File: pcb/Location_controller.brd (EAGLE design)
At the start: 75 x 48 mm, 45 parts, among them IC1 LIS302DL

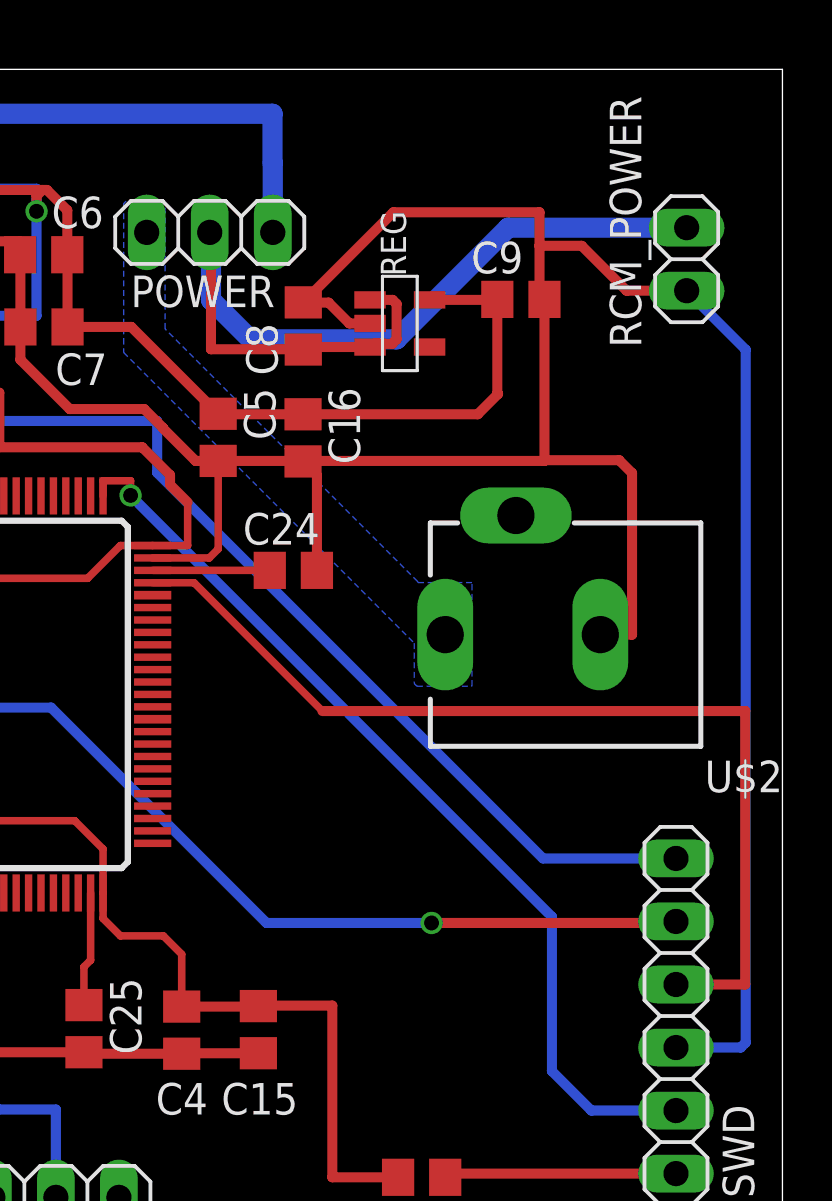
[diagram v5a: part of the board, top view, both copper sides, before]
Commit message: Add PWR and ERR indicator LEDs
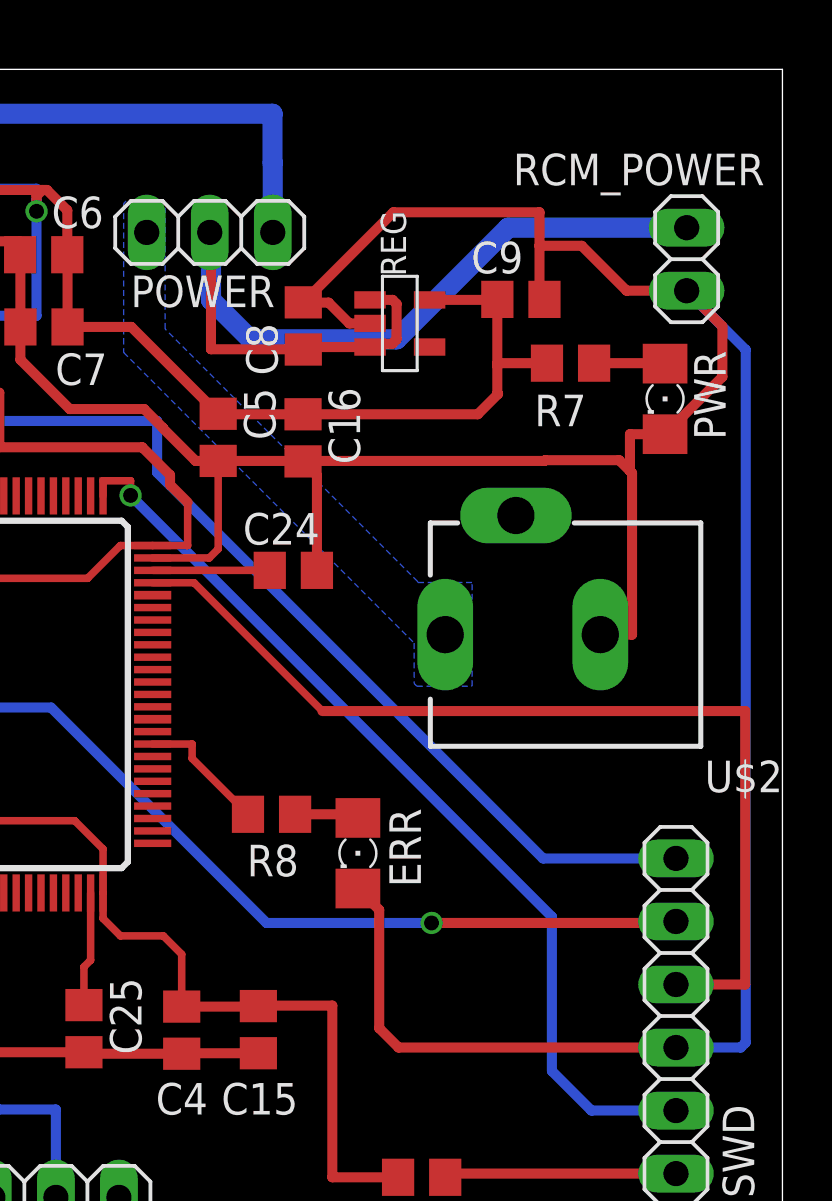
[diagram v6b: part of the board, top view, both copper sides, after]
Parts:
- added ERR, PWR: (no value), eagle-ltspice:LED_1206
- added R7, R8: 68, eagle-ltspice:R0805
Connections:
- new net N$12: PWR.A, R7.1
- new net N$13: ERR.A, R8.1
- new net N$14: R8.2, U$1.59
- net GND: now also ERR.C, PWR.C
- net VDD: now also R7.2
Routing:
- net GND: track 324.7 -> 346.7 mm
- net N$14: track 0.00 -> 5.35 mm
- net N$12: track 0.00 -> 2.88 mm
- net N$13: track 0.00 -> 2.59 mm
- net VDD: track 272.9 -> 274.9 mm
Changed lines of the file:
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@@
 </element>
 <element name="RCM_POWER" library="pinhead" package="1X02" value="" x="71.14" y="40.35" smashed="yes" rot="R90">
-<attribute name="NAME" x="69.3112" y="36.7938" size="1.27" layer="25" ratio="10" rot="R90"/>
+<attribute name="NAME" x="74.2762" y="44.6012" size="1.27" layer="25" ratio="10" rot="R180"/>
 <attribute name="VALUE" x="74.315" y="37.81" size="1.27" layer="27" rot="R90"/>
 </element>
@@
 <element name="JP2" library="pinhead" package="1X06" value="" x="25.4" y="2.54"/>
 <element name="JP3" library="pinhead" package="1X06" value="" x="8.89" y="2.54"/>
+<element name="PWR" library="eagle-ltspice" package="LED_1206" value="" x="70.27" y="34.72" smashed="yes" rot="R270">
+<attribute name="SPICEMODEL" value="NONE" x="70.27" y="34.72" size="1.778" layer="27" rot="R270" display="off"/>
+<attribute name="SPICETYPE" value="diode" x="70.27" y="34.72" size="1.778" layer="27" rot="R270" display="off"/>
+<attribute name="SPICEPREFIX" value="D" x="70.27" y="34.72" size="1.778" layer="27" rot="R270" display="off"/>
+<attribute name="NAME" x="71.44" y="36.66" size="1.27" layer="25" rot="R270"/>
+<attribute name="VALUE" x="67.73" y="35.99" size="1.27" layer="27" rot="R270"/>
+</element>
+<element name="R7" library="eagle-ltspice" package="R0805" value="68" x="66.46" y="36.16" rot="R180">
+<attribute name="SPICEMODEL" value="NONE" x="66.46" y="36.16" size="1.778" layer="27" rot="R180" display="off"/>
+<attribute name="SPICEPREFIX" value="R" x="66.46" y="36.16" size="1.778" layer="27" rot="R180" display="off"/>
+</element>
+<element name="R8" library="eagle-ltspice" package="R0805" value="68" x="54.41" y="17.98" smashed="yes" rot="R180">
+<attribute name="SPICEMODEL" value="NONE" x="54.41" y="17.98" size="1.778" layer="27" rot="R180" display="off"/>
+<attribute name="SPICEPREFIX" value="R" x="54.41" y="17.98" size="1.778" layer="27" rot="R180" display="off"/>
+<attribute name="NAME" x="55.505" y="16.75" size="1.27" layer="25" rot="R180"/>
+<attribute name="VALUE" x="55.045" y="20.52" size="1.27" layer="27" rot="R180"/>
+</element>
+<element name="ERR" library="eagle-ltspice" package="LED_1206" value="" x="57.89" y="16.41" smashed="yes" rot="R270">
+<attribute name="SPICEMODEL" value="NONE" x="57.89" y="16.41" size="1.778" layer="27" rot="R270" display="off"/>
+<attribute name="SPICETYPE" value="diode" x="57.89" y="16.41" size="1.778" layer="27" rot="R270" display="off"/>
+<attribute name="SPICEPREFIX" value="D" x="57.89" y="16.41" size="1.778" layer="27" rot="R270" display="off"/>
+<attribute name="NAME" x="59.16" y="18.22" size="1.27" layer="25" rot="R270"/>
+<attribute name="VALUE" x="55.35" y="17.68" size="1.27" layer="27" rot="R270"/>
+</element>
 </elements>
 <signals>
@@
 <wire x1="65.21" y1="40.89" x2="65.21" y2="38.93" width="0.4064" layer="1"/>
 <wire x1="65.21" y1="38.93" x2="65.41" y2="38.73" width="0.4064" layer="1"/>
-<wire x1="65.41" y1="32.22" x2="65.41" y2="38.73" width="0.4064" layer="1"/>
 <wire x1="71.14" y1="39.08" x2="68.72" y2="39.08" width="0.4064" layer="1"/>
 <wire x1="68.72" y1="39.08" x2="66.91" y2="40.89" width="0.4064" layer="1"/>
@@
 <wire x1="65.41" y1="32.22" x2="65.44" y2="32.25" width="0.4064" layer="1"/>
 <wire x1="65.44" y1="32.25" x2="68.42" y2="32.25" width="0.4064" layer="1"/>
-<wire x1="68.42" y1="32.25" x2="68.94" y2="31.73" width="0.4064" layer="1"/>
+<wire x1="68.42" y1="32.25" x2="68.855" y2="31.815" width="0.4064" layer="1"/>
+<wire x1="68.855" y1="31.815" x2="68.94" y2="31.73" width="0.4064" layer="1"/>
 <wire x1="68.94" y1="31.73" x2="68.94" y2="25.22" width="0.4064" layer="1"/>
 <wire x1="68.94" y1="25.22" x2="67.66" y2="25.22" width="0.4064" layer="1"/>
@@
 <wire x1="34.52" y1="42.39" x2="34.52" y2="42.17" width="0.4064" layer="1"/>
 <wire x1="40.18" y1="39.39" x2="41.79" y2="39.39" width="0.4064" layer="1"/>
+<contactref element="PWR" pad="C"/>
+<wire x1="70.27" y1="33.298" x2="68.855" y2="33.298" width="0.4064" layer="1"/>
+<wire x1="68.855" y1="33.298" x2="68.855" y2="31.815" width="0.4064" layer="1"/>
+<wire x1="70.27" y1="33.298" x2="72.58" y2="35.608" width="0.4064" layer="1"/>
+<wire x1="72.58" y1="35.608" x2="72.58" y2="37.64" width="0.4064" layer="1"/>
+<wire x1="72.58" y1="37.64" x2="71.14" y2="39.08" width="0.4064" layer="1"/>
+<contactref element="ERR" pad="C"/>
+<wire x1="57.89" y1="14.988" x2="58.75" y2="14.128" width="0.4064" layer="1"/>
+<wire x1="58.75" y1="14.128" x2="58.75" y2="9.36" width="0.4064" layer="1"/>
+<wire x1="58.75" y1="9.36" x2="59.53" y2="8.58" width="0.4064" layer="1"/>
+<wire x1="59.53" y1="8.58" x2="70.71" y2="8.58" width="0.4064" layer="1"/>
 </signal>
 <signal name="N$1">
@@
 <wire x1="55.68" y1="34.1" x2="62.72" y2="34.1" width="0.4064" layer="1"/>
 <wire x1="62.72" y1="34.1" x2="63.54" y2="34.92" width="0.4064" layer="1"/>
-<wire x1="63.51" y1="38.73" x2="63.51" y2="34.95" width="0.4064" layer="1"/>
+<wire x1="63.51" y1="38.73" x2="63.51" y2="36.16" width="0.4064" layer="1"/>
+<wire x1="63.51" y1="36.04" x2="63.51" y2="34.95" width="0.4064" layer="1"/>
 <wire x1="63.51" y1="34.95" x2="63.54" y2="34.92" width="0.4064" layer="1"/>
 <wire x1="51.03" y1="30.55" x2="50.32" y2="31.26" width="0.4064" layer="1"/>
@@
 <wire x1="59.51" y1="3.35" x2="56.86" y2="3.35" width="0.4064" layer="1"/>
 <wire x1="56.86" y1="3.35" x2="56.86" y2="10.27" width="0.4064" layer="1"/>
+<contactref element="R7" pad="2"/>
+<wire x1="65.51" y1="36.16" x2="63.51" y2="36.16" width="0.4064" layer="1"/>
+<wire x1="63.51" y1="36.16" x2="63.51" y2="36.04" width="0.4064" layer="1"/>
 </signal>
 <signal name="I2C_SCL">
@@
 <contactref element="U$2" pad="GNDBREAK"/>
 </signal>
+<signal name="N$12">
+<contactref element="PWR" pad="A"/>
+<contactref element="R7" pad="1"/>
+<wire x1="67.41" y1="36.16" x2="70.27" y2="36.16" width="0.4064" layer="1"/>
+<wire x1="70.27" y1="36.16" x2="70.27" y2="36.142" width="0.4064" layer="1"/>
+</signal>
+<signal name="N$13">
+<contactref element="ERR" pad="A"/>
+<contactref element="R8" pad="1"/>
+<wire x1="57.89" y1="17.832" x2="57.742" y2="17.98" width="0.4064" layer="1"/>
+<wire x1="57.742" y1="17.98" x2="55.36" y2="17.98" width="0.4064" layer="1"/>
+</signal>
+<signal name="N$14">
+<contactref element="R8" pad="2"/>
+<contactref element="U$1" pad="59"/>
+<wire x1="53.46" y1="17.98" x2="51.21" y2="20.23" width="0.3048" layer="1"/>
+<wire x1="51.21" y1="20.23" x2="51.21" y2="20.81" width="0.3048" layer="1"/>
+<wire x1="51.21" y1="20.81" x2="49.62" y2="20.81" width="0.3048" layer="1"/>
+</signal>
 </signals>

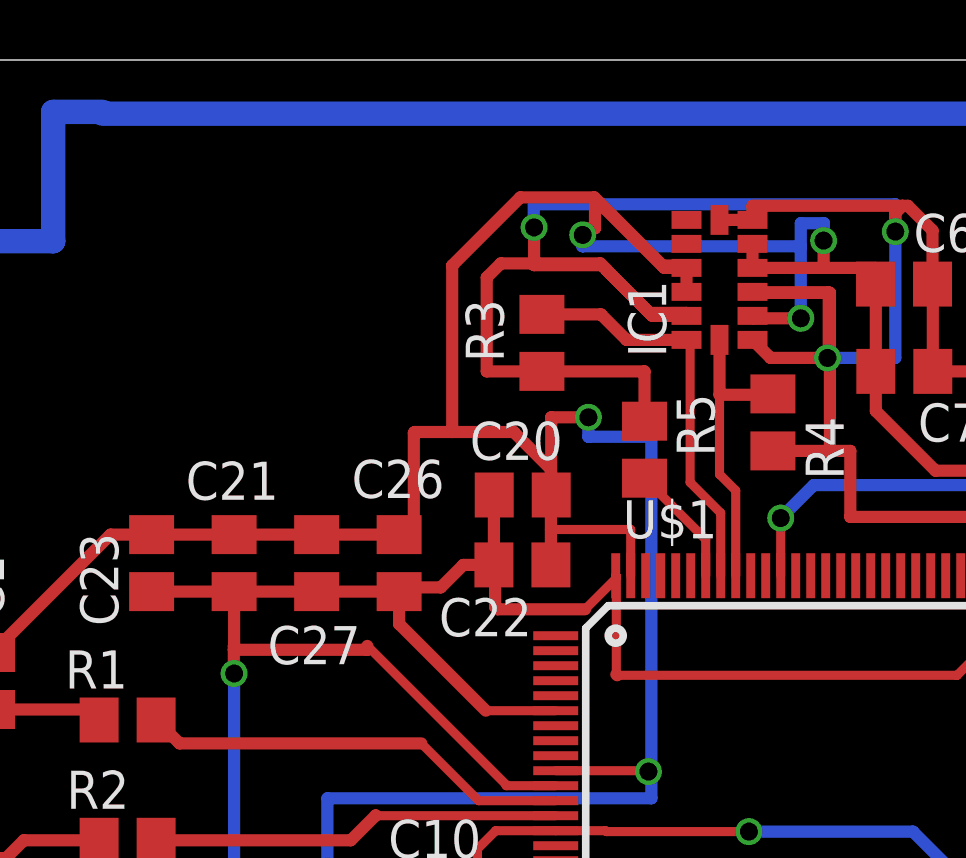
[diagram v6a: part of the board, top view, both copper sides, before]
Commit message: Add I2C debug pins
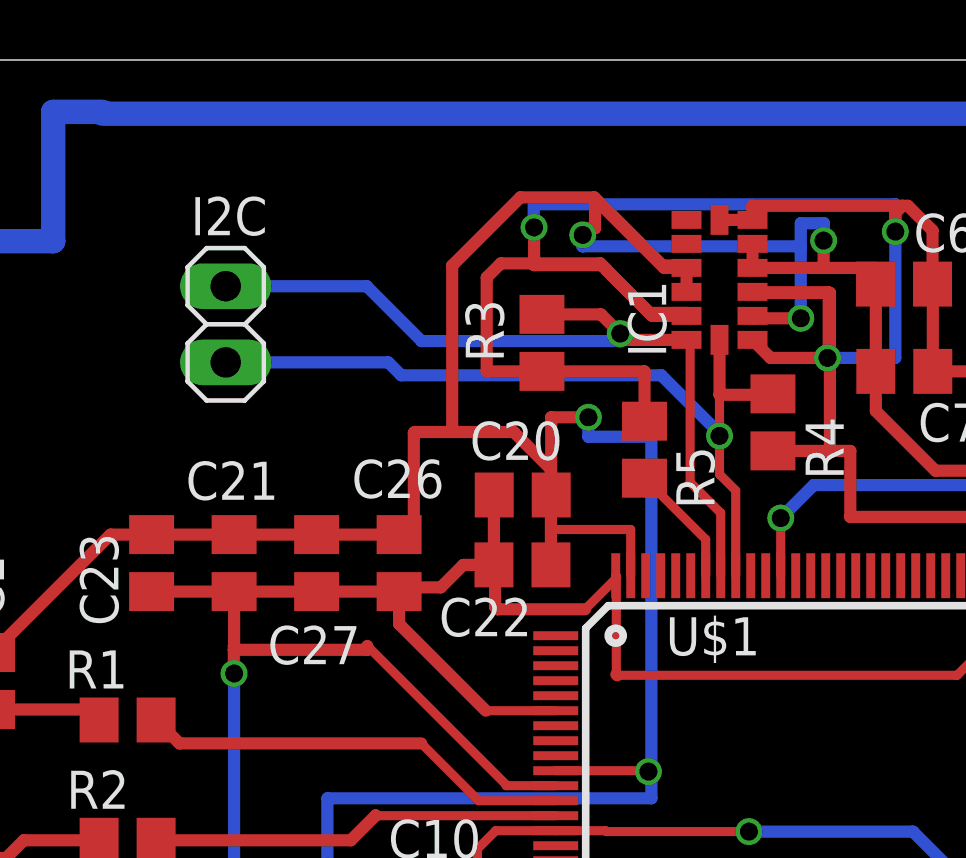
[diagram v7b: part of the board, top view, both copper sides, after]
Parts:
- added I2C: (no value), pinhead:1X02
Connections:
- net I2C_SCL: now also I2C.2
- net I2C_SDA: now also I2C.1
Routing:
- net I2C_SCL: track 9.89 -> 27.4 mm, vias 0 -> 1
- net I2C_SDA: track 13.5 -> 27.8 mm, vias 0 -> 1
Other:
- board text added: "SCL"
- board text added: "SDA"
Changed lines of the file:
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@@
 <text x="69.11" y="14.57" size="1.778" layer="51" rot="R180">NRST</text>
 <text x="69.13" y="17.13" size="1.778" layer="51" rot="R180">SWO</text>
+<text x="15.75" y="39.72" size="1.778" layer="52">SDA</text>
+<text x="15.75" y="37.11" size="1.778" layer="52">SCL</text>
 </plain>
 <attributes>
@@
 </autorouter>
 <elements>
-<element name="U$1" library="stm32f4" package="TQFP100" value="STM32F407V" x="41.62" y="22.81"/>
+<element name="U$1" library="stm32f4" package="TQFP100" value="STM32F407V" x="41.62" y="22.81" smashed="yes">
+<attribute name="NAME" x="37.29" y="28.1551" size="1.27" layer="25"/>
+<attribute name="VALUE" x="36.5349" y="23.7051" size="1.27" layer="27"/>
+</element>
 <element name="Q1" library="crystal" package="HC49/S" value="" x="9.99" y="23.73" rot="R90">
 <attribute name="OC_NEWARK" value="unknown" x="9.99" y="23.73" size="1.778" layer="27" rot="R90" display="off"/>
@@
 <attribute name="SPICEMODEL" value="NONE" x="36.58" y="35.01" size="1.778" layer="27" rot="R270" display="off"/>
 <attribute name="SPICEPREFIX" value="R" x="36.58" y="35.01" size="1.778" layer="27" rot="R270" display="off"/>
-<attribute name="NAME" x="37.65" y="36.875" size="1.27" layer="25" rot="R270"/>
+<attribute name="NAME" x="37.64" y="35.125" size="1.27" layer="25" rot="R270"/>
 <attribute name="VALUE" x="34.04" y="35.645" size="1.27" layer="27" rot="R270"/>
 </element>
@@
 <attribute name="NAME" x="59.16" y="18.22" size="1.27" layer="25" rot="R270"/>
 <attribute name="VALUE" x="55.35" y="17.68" size="1.27" layer="27" rot="R270"/>
+</element>
+<element name="I2C" library="pinhead" package="1X02" value="" x="22.62" y="39.19" smashed="yes" rot="R270">
+<attribute name="NAME" x="21.4538" y="42.1588" size="1.27" layer="25" ratio="10"/>
+<attribute name="VALUE" x="19.445" y="41.73" size="1.27" layer="27" rot="R270"/>
 </element>
 </elements>
@@
 <contactref element="R4" pad="2"/>
 <wire x1="39.08" y1="38.67" x2="39.08" y2="36.84" width="0.4064" layer="1"/>
-<wire x1="39.08" y1="36.84" x2="39.08" y2="34.19" width="0.3048" layer="1"/>
+<wire x1="39.08" y1="36.84" x2="39.08" y2="35.47" width="0.3048" layer="1"/>
+<wire x1="39.08" y1="35.18" x2="39.08" y2="34.19" width="0.3048" layer="1"/>
 <wire x1="39.08" y1="34.19" x2="39.62" y2="33.65" width="0.3048" layer="1"/>
 <wire x1="39.62" y1="33.65" x2="39.62" y2="30.81" width="0.3048" layer="1"/>
 <wire x1="40.86" y1="36.87" x2="40.86" y2="36.84" width="0.4064" layer="1"/>
 <wire x1="40.86" y1="36.84" x2="39.08" y2="36.84" width="0.4064" layer="1"/>
+<contactref element="I2C" pad="2"/>
+<wire x1="22.62" y1="37.92" x2="28.04" y2="37.92" width="0.4064" layer="16"/>
+<wire x1="28.04" y1="37.92" x2="28.47" y2="37.49" width="0.4064" layer="16"/>
+<wire x1="28.47" y1="37.49" x2="37.14" y2="37.49" width="0.4064" layer="16"/>
+<wire x1="37.14" y1="37.49" x2="39.08" y2="35.55" width="0.4064" layer="16"/>
+<wire x1="39.08" y1="35.55" x2="39.08" y2="35.47" width="0.4064" layer="16"/>
+<via x="39.08" y="35.47" extent="1-16" drill="0.6" shape="square"/>
+<wire x1="39.08" y1="35.47" x2="39.08" y2="35.18" width="0.4064" layer="1"/>
 </signal>
 <signal name="I2C_SDA">
@@
 <wire x1="38.1" y1="38.55" x2="37.98" y2="38.67" width="0.4064" layer="1"/>
 <wire x1="33.16" y1="39.52" x2="35.13" y2="39.52" width="0.4064" layer="1"/>
-<wire x1="35.13" y1="39.52" x2="35.98" y2="38.67" width="0.4064" layer="1"/>
+<wire x1="35.77" y1="38.88" x2="35.98" y2="38.67" width="0.4064" layer="1"/>
 <wire x1="35.98" y1="38.67" x2="37.98" y2="38.67" width="0.4064" layer="1"/>
+<contactref element="I2C" pad="1"/>
+<wire x1="35.77" y1="38.61" x2="35.77" y2="38.88" width="0.4064" layer="16"/>
+<via x="35.77" y="38.88" extent="1-16" drill="0.6" shape="square"/>
+<wire x1="35.77" y1="38.88" x2="35.13" y2="39.52" width="0.4064" layer="1"/>
+<wire x1="22.62" y1="40.46" x2="27.32" y2="40.46" width="0.4064" layer="16"/>
+<wire x1="27.32" y1="40.46" x2="29.15" y2="38.63" width="0.4064" layer="16"/>
+<wire x1="29.15" y1="38.63" x2="35.52" y2="38.63" width="0.4064" layer="16"/>
+<wire x1="35.52" y1="38.63" x2="35.77" y2="38.88" width="0.4064" layer="16"/>
 </signal>
 <signal name="N$8">
